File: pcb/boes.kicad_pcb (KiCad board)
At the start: 2 copper layers, 18 parts, among them J1 SW_A, J10 HUB75 Display ctrl, J2 SW_B, J3 SW_C, J4 Pot_J, J5 Pot_P, J6 Sens_J, J7 Sens_P, J8 Buzzer, J9 Display power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

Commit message: Main PCB ready for final tweaks
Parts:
- moved H4 25.1 mm to (157.5, 129.5)
- moved Q1 22.6 mm to (135.4, 118.4)
- moved R1 22.6 mm to (132.3, 118.4)
- moved R2 21.3 mm to (139.2, 118.4)
- moved H3 19.3 mm to (101.6, 129.5)
- moved H2 18.3 mm to (160.0, 55.9)
- moved J2 16.3 mm to (147.5, 114.3)
- moved J3 16.3 mm to (147.4, 121.9)
- moved J5 16.3 mm to (144.8, 78.7)
- moved J7 16.3 mm to (144.8, 96.5)
- moved J1 16.3 mm to (147.5, 106.7)
- moved J4 16.3 mm to (144.8, 71.1)
- moved J6 16.3 mm to (144.8, 88.9)
- moved J9 14.4 mm to (147.3, 63.5)
- moved J10 12.7 mm to (99.1, 76.1)
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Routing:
- net OE: track 0.00 -> 22.7 mm
- net R1: track 0.00 -> 22.6 mm
- net CLK: track 0.00 -> 21.5 mm
- net R2: track 0.00 -> 20.5 mm
- net B1: track 0.00 -> 20.5 mm
- net C: track 0.00 -> 19.4 mm
- net B2: track 0.00 -> 19.4 mm
- net Latch: track 0.00 -> 19.1 mm
- net G1: track 0.00 -> 19.0 mm
- net A: track 0.00 -> 18.4 mm
- net D: track 0.00 -> 18.0 mm
- net G2: track 0.00 -> 16.9 mm
- net B: track 0.00 -> 15.9 mm
- net E: track 0.00 -> 14.9 mm
- net Buzzer: track 0.00 -> 2.51 mm
- added copper zone on F.Cu, net (none)
- added copper zone on B.Cu, net GND
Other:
- board outline added: 71.1 x 86.4 mm
- board text added: "Buzzer"
- board text added: "Börne's Bøs ${PCB_REV} ${PCB_DATE}"
- board text added: "Display"
- board text added: "S"
- board text removed: "Display Power"

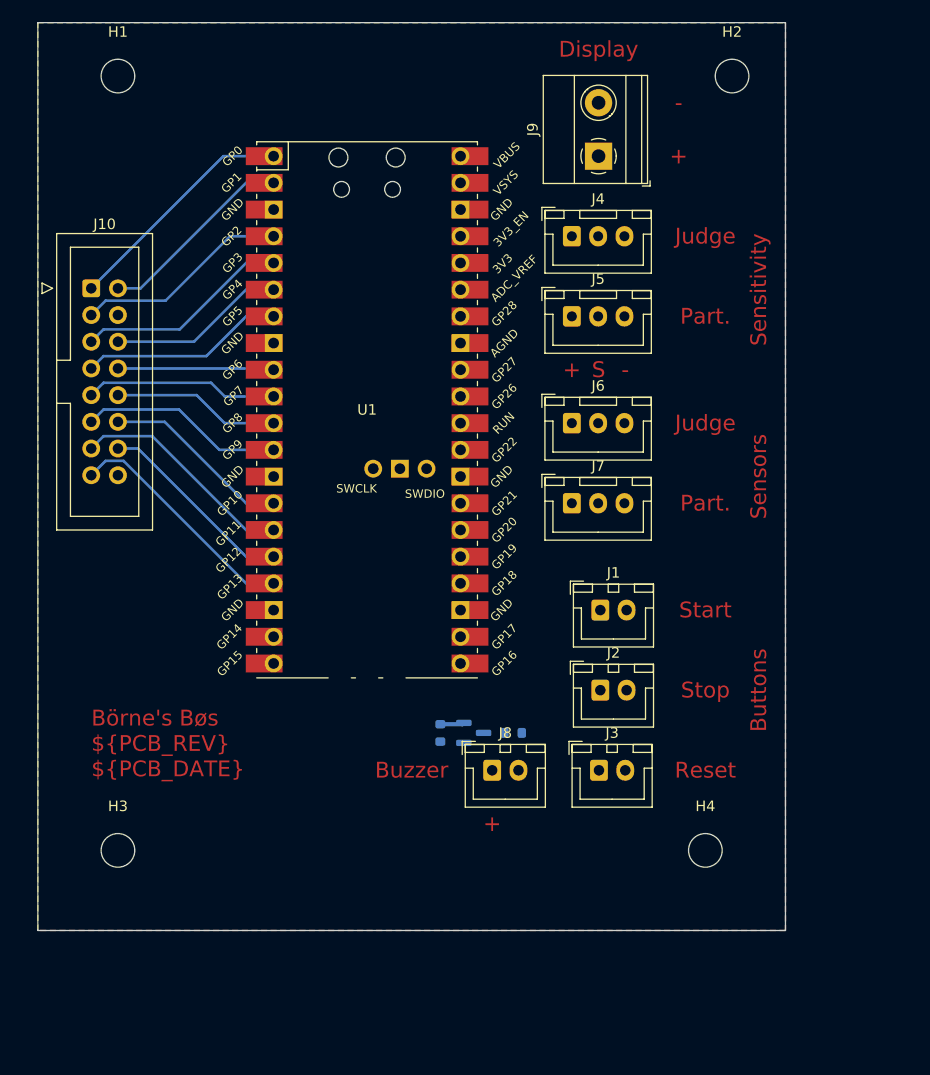
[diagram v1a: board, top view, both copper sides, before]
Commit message: Slim main PCB
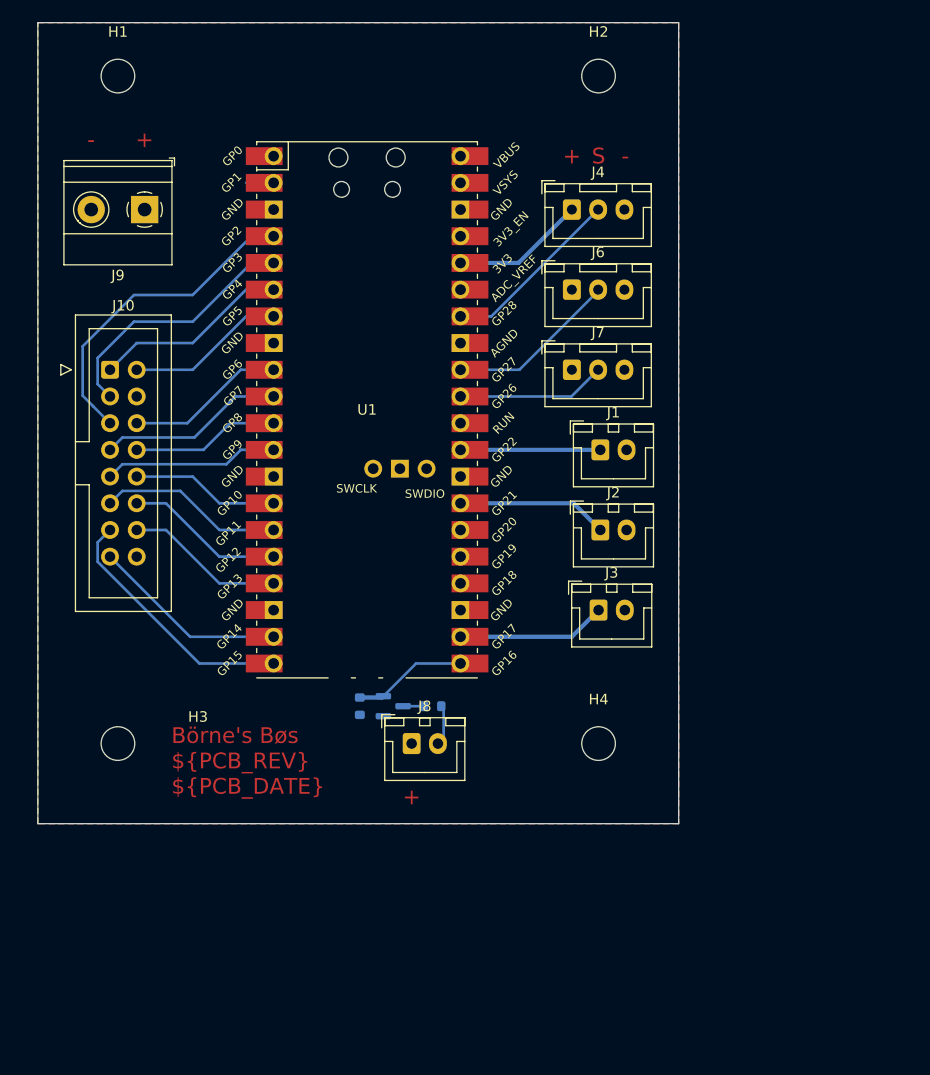
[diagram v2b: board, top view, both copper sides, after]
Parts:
- removed J5: Pot_P, Connector_JST:JST_XH_B3B-XH-A_1x03_P2.50mm_Vertical
- moved J9 43.5 mm to (104.1, 68.6), turned to 180 degrees
- moved J3 15.2 mm to (147.3, 106.7)
- moved J1 15.2 mm to (147.5, 91.4)
- moved J2 15.2 mm to (147.5, 99.1)
- moved H4 14.4 mm to (147.3, 119.4)
- moved H2 12.7 mm to (147.3, 55.9)
- moved J6 12.7 mm to (144.8, 76.2)
- moved J7 12.7 mm to (144.8, 83.8)
- moved H3 10.2 mm to (101.6, 119.4)
- moved R1 8.07 mm to (124.6, 115.8)
- moved J8 8.07 mm to (129.5, 119.4)
- moved Q1 8.07 mm to (127.8, 115.8)
- moved R2 8.07 mm to (131.5, 115.8)
- moved J10 7.95 mm to (100.8, 83.8)
- moved J4 2.54 mm to (144.8, 68.6)
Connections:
- J4 pad 2: Pot_J -> Pot
- U1 pad 1: R1 -> unconnected-(U1-Pad1)
- U1 pad 10: A -> B2
- U1 pad 11: B -> E
- U1 pad 12: C -> A
- U1 pad 14: D -> B
- U1 pad 15: CLK -> C
- U1 pad 16: Latch -> D
- U1 pad 17: OE -> Latch
- U1 pad 19: unconnected-(U1-Pad19) -> OE
- U1 pad 2: G1 -> unconnected-(U1-Pad2)
- U1 pad 20: unconnected-(U1-Pad20) -> CLK
- U1 pad 24: Stop -> unconnected-(U1-Pad24)
- U1 pad 25: Start -> unconnected-(U1-Pad25)
- U1 pad 27: unconnected-(U1-Pad27) -> Stop
- U1 pad 29: unconnected-(U1-Pad29) -> Start
- U1 pad 34: unconnected-(U1-Pad34) -> Pot
- U1 pad 4: B1 -> R2
- U1 pad 5: R2 -> B1
- U1 pad 6: G2 -> R1
- U1 pad 7: B2 -> G1
- U1 pad 9: E -> G2
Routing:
- net Pot: track 0.00 -> 17.3 mm
- net Sens_J: track 0.00 -> 16.3 mm
- net Stop: track 0.00 -> 14.4 mm
- net Reset: track 0.00 -> 14.2 mm
- net Sens_P: track 0.00 -> 14.1 mm
- net Start: track 0.00 -> 13.3 mm
- net +3V3: track 0.00 -> 12.7 mm
- net R2: track 20.5 -> 30.9 mm
- net Buzzer: track 2.51 -> 11.1 mm
- net B1: track 20.5 -> 24.6 mm
- net OE: track 22.7 -> 18.7 mm
- net Latch: track 19.1 -> 15.1 mm
- net Net-(J8-Pad2): track 0.00 -> 3.88 mm
- net R1: track 22.6 -> 18.7 mm
- net G1: track 19.0 -> 15.1 mm
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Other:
- board size 71.1 x 86.4 mm -> 61 x 76.2 mm
- board text removed: "Buttons"
- board text removed: "Buzzer"
- board text removed: "Display"
- board text removed: "Judge"
- board text removed: "Part."
- board text removed: "Reset"
- board text removed: "Sensitivity"
- board text removed: "Sensors"
- board text removed: "Start"
- board text removed: "Stop"
